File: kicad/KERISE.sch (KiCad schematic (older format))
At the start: 4 parts, among them SW1 RESET, U1 ESP32-PICO-D4

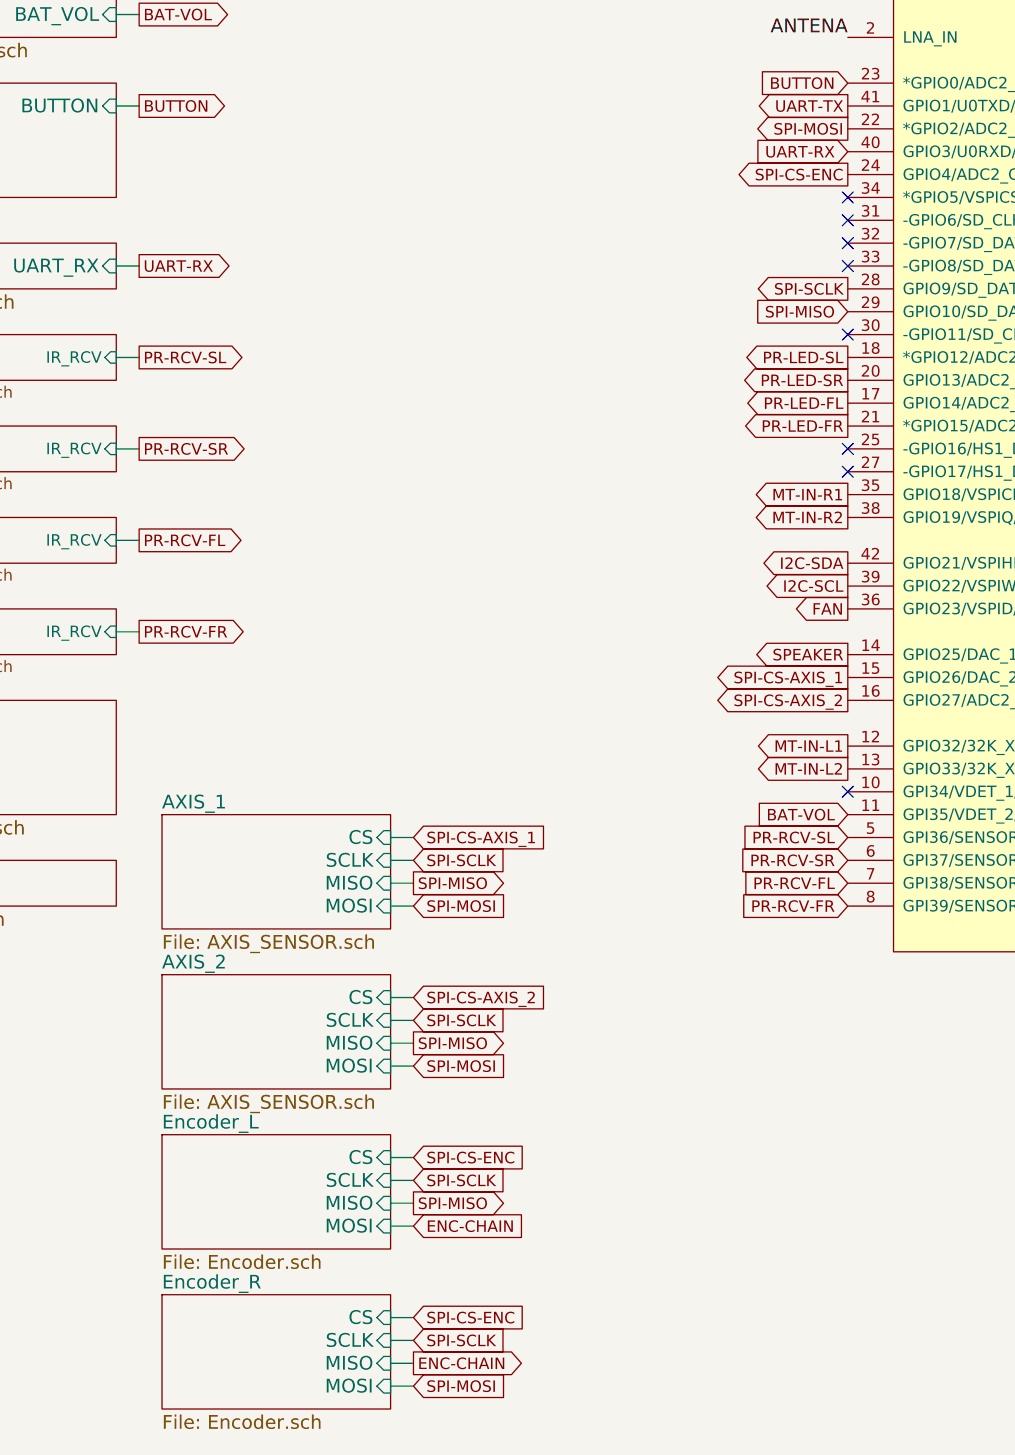
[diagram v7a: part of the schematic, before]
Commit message: 回路にMA702を追加
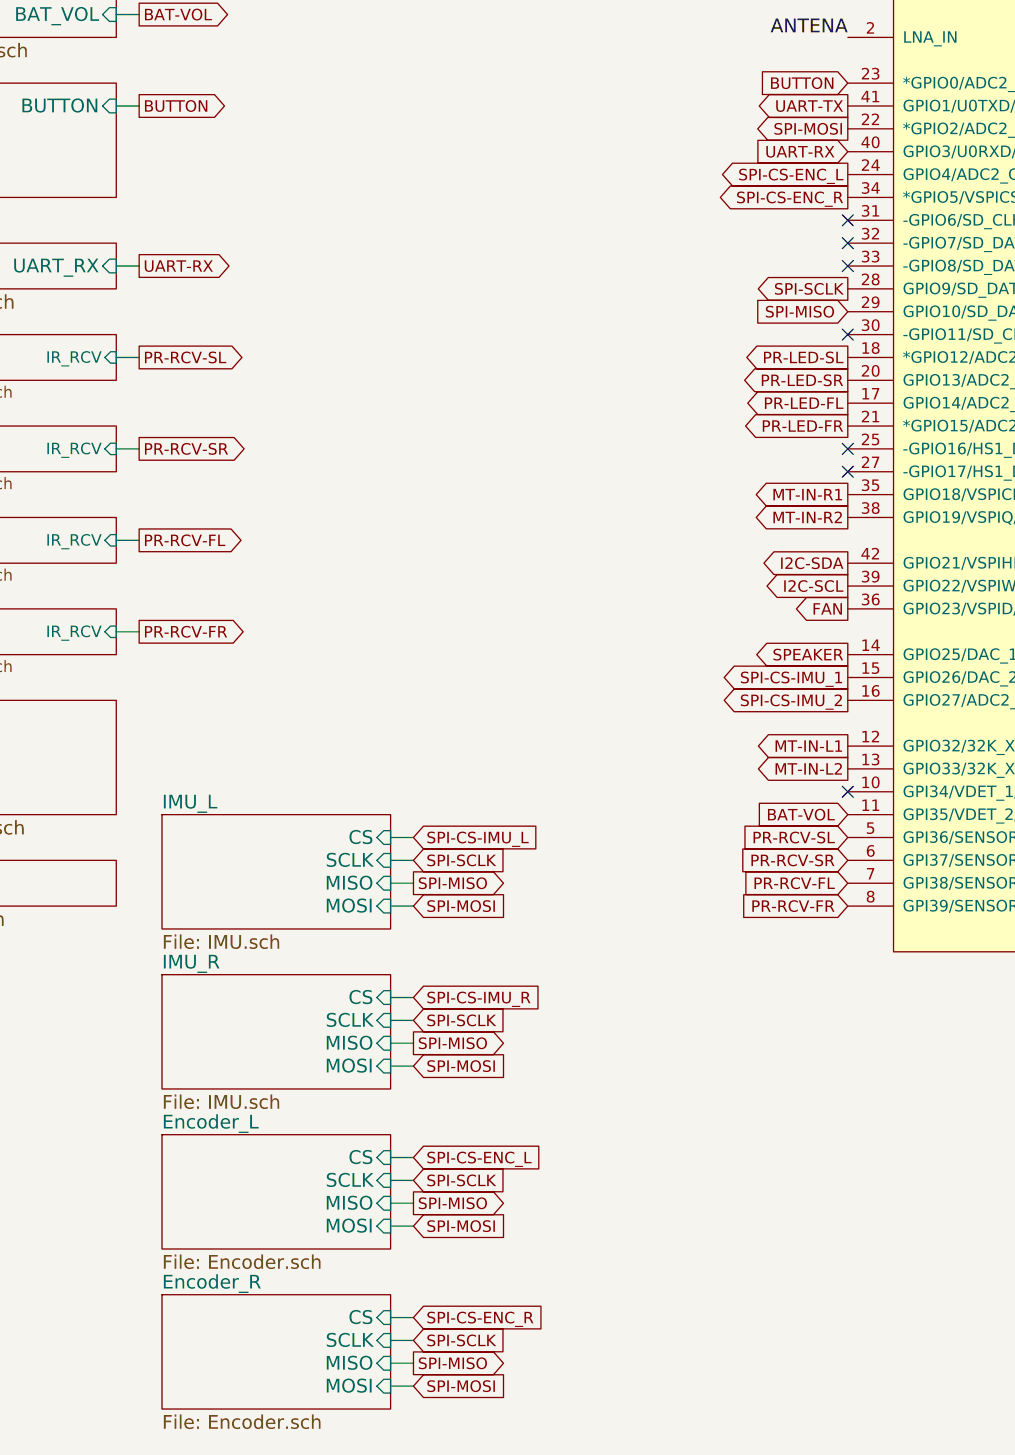
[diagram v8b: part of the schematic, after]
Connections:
- net SPI-CS-ENC_R: now reaches U1.34 (*GPIO5/VSPICS0/HS1_DATA6/EMAC_RX_CLK)
- net SPI-CS-AXIS_1 renamed SPI-CS-IMU_1
- net SPI-CS-AXIS_2 renamed SPI-CS-IMU_2
- net SPI-CS-ENC renamed SPI-CS-ENC_L
- no-connect marks 13 -> 12
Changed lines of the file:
@@
 SPI-MOSI
 Text GLabel 3700 5900 2    50   Input ~ 0
-SPI-CS-ENC
+SPI-CS-ENC_L
 Text GLabel 3700 6600 2    50   Input ~ 0
-SPI-CS-ENC
-Text GLabel 3700 6200 2    50   Input ~ 0
-ENC-CHAIN
-Text GLabel 3700 6800 2    50   Output ~ 0
-ENC-CHAIN
+SPI-CS-ENC_R
 Text GLabel 3700 6700 2    50   Input ~ 0
 SPI-SCLK
@@
 S 2600 5100 1000 500
 U 57CC33F6
-F0 "AXIS_2" 60
-F1 "AXIS_SENSOR.sch" 60
+F0 "IMU_R" 60
+F1 "IMU.sch" 60
 F2 "MISO" I R 3600 5400 60
 F3 "MOSI" I R 3600 5500 60
@@
 SPI-SCLK
 Text GLabel 3700 5200 2    50   Input ~ 0
-SPI-CS-AXIS_2
+SPI-CS-IMU_R
 Text GLabel 3700 5400 2    50   Output ~ 0
 SPI-MISO
@@
 SPI-MOSI
 Text GLabel 5600 3800 0    50   Output ~ 0
-SPI-CS-AXIS_1
+SPI-CS-IMU_1
 Text GLabel 5600 1600 0    50   Output ~ 0
-SPI-CS-ENC
+SPI-CS-ENC_L
 Text GLabel 5600 2100 0    50   Output ~ 0
 SPI-SCLK
@@
 S 2600 4400 1000 500
 U 5A18D4D6
-F0 "AXIS_1" 60
-F1 "AXIS_SENSOR.sch" 60
+F0 "IMU_L" 60
+F1 "IMU.sch" 60
 F2 "MISO" I R 3600 4700 60
 F3 "MOSI" I R 3600 4800 60
@@
 SPI-SCLK
 Text GLabel 3700 4500 2    50   Input ~ 0
-SPI-CS-AXIS_1
+SPI-CS-IMU_L
 Text GLabel 3700 4700 2    50   Output ~ 0
 SPI-MISO
@@
 SPI-MOSI
 Text GLabel 5600 3900 0    50   Output ~ 0
-SPI-CS-AXIS_2
+SPI-CS-IMU_2
 NoConn ~ 9600 2600
 NoConn ~ 5600 1800
@@
 	1    0    0    -1
 $EndComp
-NoConn ~ 5600 1700
 Wire Wire Line
 	9700 3100 9600 3100
@@
 	1    0    0    -1
 $EndComp
+Text GLabel 5600 1700 0    50   Output ~ 0
+SPI-CS-ENC_R
+Text GLabel 3700 6800 2    50   Output ~ 0
+SPI-MISO
+Text GLabel 3700 6200 2    50   Input ~ 0
+SPI-MOSI
 $EndSCHEMATC
